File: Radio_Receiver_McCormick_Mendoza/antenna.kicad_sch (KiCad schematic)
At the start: 31 parts, among them J33 XFIL_IN, J34 XFIL_OUT, J45 CENTER_TAP, J5 Conn_Coaxial, J5 FIL_IN, J8 FIL_OUT, T1 Transformer_1P_SS, U13 SN74CBT3253CDBR

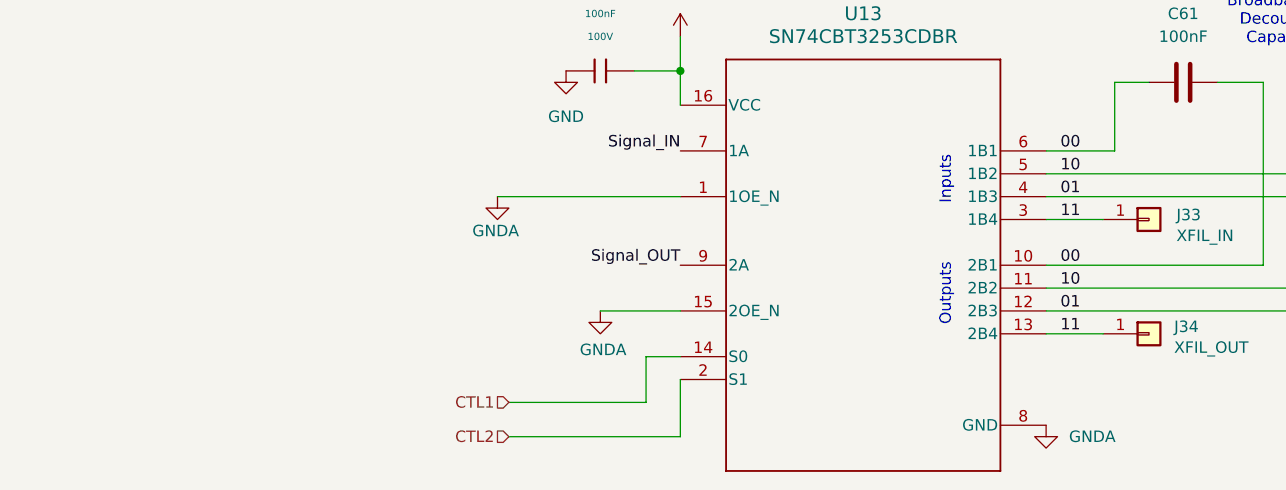
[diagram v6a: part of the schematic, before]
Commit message: Swapped voltage regulator to output 4.5V
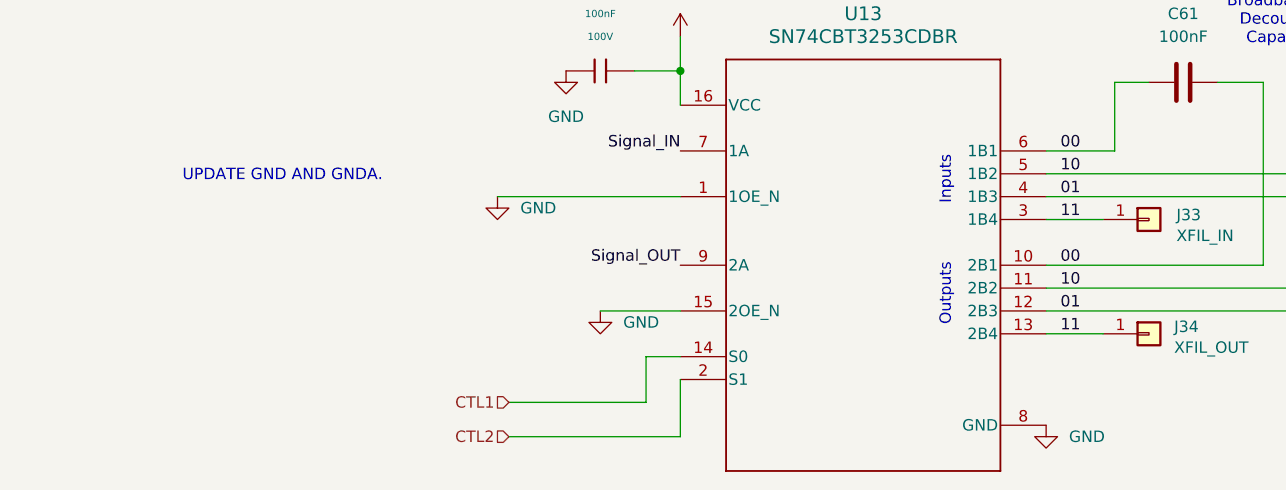
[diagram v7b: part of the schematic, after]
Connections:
- net GND: now also U13.1 (1OE_N), U13.15 (2OE_N), U13.8 (GND)
- net GNDA: no longer U13.1 (1OE_N), U13.15 (2OE_N), U13.8 (GND)
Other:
- note added: "UPDATE GND AND GNDA."
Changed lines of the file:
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@@
 		)
 	)
+	(text "UPDATE GND AND GNDA."
+		(exclude_from_sim no)
+		(at 62.484 118.364 0)
+		(effects
+			(font
+				(size 1.27 1.27)
+			)
+		)
+	)
 	(text "GNDA is the Antenna Ground\nIt must be separate from the\ndevice ground (GND) to prevent\nground loops."
 		(exclude_from_sim no)
@@
 	)
 	(symbol
-		(lib_id "power:GND")
-		(at 97.79 133.35 0)
-		(unit 1)
-		(body_style 1)
-		(exclude_from_sim no)
-		(in_bom yes)
-		(on_board yes)
-		(in_pos_files yes)
-		(dnp no)
-		(property "Reference" "#PWR012"
-			(at 97.79 139.7 0)
-			(hide yes)
-			(show_name no)
-			(do_not_autoplace no)
-			(effects
-				(font
-					(size 1.27 1.27)
-				)
-			)
-		)
-		(property "Value" "GNDA"
-			(at 95.504 137.668 0)
-			(show_name no)
-			(do_not_autoplace no)
-			(effects
-				(font
-					(size 1.27 1.27)
-				)
-				(justify left)
-			)
-		)
-		(property "Footprint" ""
-			(at 97.79 133.35 0)
-			(hide yes)
-			(show_name no)
-			(do_not_autoplace no)
-			(effects
-				(font
-					(size 1.27 1.27)
-				)
-			)
-		)
-		(property "Datasheet" ""
-			(at 97.79 133.35 0)
-			(hide yes)
-			(show_name no)
-			(do_not_autoplace no)
-			(effects
-				(font
-					(size 1.27 1.27)
-				)
-			)
-		)
-		(property "Description" "Power symbol creates a global label with name \"GND\" , ground"
-			(at 97.79 133.35 0)
-			(hide yes)
-			(show_name no)
-			(do_not_autoplace no)
-			(effects
-				(font
-					(size 1.27 1.27)
-				)
-			)
-		)
-		(pin "1"
-		)
-		(instances
-			(project "Radio_Receiver_McCormick_Mendoza"
-				(path "/f31d31ab-6846-4f3a-92b1-aa5a6a13373f/bb2f90fe-90d6-4041-8023-4e8a6153d0ef"
-					(reference "#PWR012")
-					(unit 1)
-				)
-			)
-		)
-	)
-	(symbol
 		(lib_id "SDRReciever-rescue:GND-power-SDRReciever-rescue")
 		(at 33.02 62.23 0)
@@
 	)
 	(symbol
+		(lib_id "power:GND")
+		(at 97.79 133.35 0)
+		(unit 1)
+		(body_style 1)
+		(exclude_from_sim no)
+		(in_bom yes)
+		(on_board yes)
+		(in_pos_files yes)
+		(dnp no)
+		(fields_autoplaced yes)
+		(property "Reference" "#PWR087"
+			(at 97.79 139.7 0)
+			(hide yes)
+			(show_name no)
+			(do_not_autoplace no)
+			(effects
+				(font
+					(size 1.27 1.27)
+				)
+			)
+		)
+		(property "Value" "GND"
+			(at 100.33 134.6199 0)
+			(show_name no)
+			(do_not_autoplace no)
+			(effects
+				(font
+					(size 1.27 1.27)
+				)
+				(justify left)
+			)
+		)
+		(property "Footprint" ""
+			(at 97.79 133.35 0)
+			(hide yes)
+			(show_name no)
+			(do_not_autoplace no)
+			(effects
+				(font
+					(size 1.27 1.27)
+				)
+			)
+		)
+		(property "Datasheet" ""
+			(at 97.79 133.35 0)
+			(hide yes)
+			(show_name no)
+			(do_not_autoplace no)
+			(effects
+				(font
+					(size 1.27 1.27)
+				)
+			)
+		)
+		(property "Description" "Power symbol creates a global label with name \"GND\" , ground"
+			(at 97.79 133.35 0)
+			(hide yes)
+			(show_name no)
+			(do_not_autoplace no)
+			(effects
+				(font
+					(size 1.27 1.27)
+				)
+			)
+		)
+		(pin "1"
+		)
+		(instances
+			(project "Radio_Receiver_McCormick_Mendoza"
+				(path "/f31d31ab-6846-4f3a-92b1-aa5a6a13373f/bb2f90fe-90d6-4041-8023-4e8a6153d0ef"
+					(reference "#PWR087")
+					(unit 1)
+				)
+			)
+		)
+	)
+	(symbol
+		(lib_id "power:GND")
+		(at 86.36 120.65 0)
+		(unit 1)
+		(body_style 1)
+		(exclude_from_sim no)
+		(in_bom yes)
+		(on_board yes)
+		(in_pos_files yes)
+		(dnp no)
+		(fields_autoplaced yes)
+		(property "Reference" "#PWR089"
+			(at 86.36 127 0)
+			(hide yes)
+			(show_name no)
+			(do_not_autoplace no)
+			(effects
+				(font
+					(size 1.27 1.27)
+				)
+			)
+		)
+		(property "Value" "GND"
+			(at 88.9 121.9199 0)
+			(show_name no)
+			(do_not_autoplace no)
+			(effects
+				(font
+					(size 1.27 1.27)
+				)
+				(justify left)
+			)
+		)
+		(property "Footprint" ""
+			(at 86.36 120.65 0)
+			(hide yes)
+			(show_name no)
+			(do_not_autoplace no)
+			(effects
+				(font
+					(size 1.27 1.27)
+				)
+			)
+		)
+		(property "Datasheet" ""
+			(at 86.36 120.65 0)
+			(hide yes)
+			(show_name no)
+			(do_not_autoplace no)
+			(effects
+				(font
+					(size 1.27 1.27)
+				)
+			)
+		)
+		(property "Description" "Power symbol creates a global label with name \"GND\" , ground"
+			(at 86.36 120.65 0)
+			(hide yes)
+			(show_name no)
+			(do_not_autoplace no)
+			(effects
+				(font
+					(size 1.27 1.27)
+				)
+			)
+		)
+		(pin "1"
+		)
+		(instances
+			(project "Radio_Receiver_McCormick_Mendoza"
+				(path "/f31d31ab-6846-4f3a-92b1-aa5a6a13373f/bb2f90fe-90d6-4041-8023-4e8a6153d0ef"
+					(reference "#PWR089")
+					(unit 1)
+				)
+			)
+		)
+	)
+	(symbol
 		(lib_id "SDRReciever-rescue:L-Device-SDRReciever-rescue")
 		(at 250.19 128.27 0)
@@
 			)
 		)
-		(property "Value" "GNDA"
+		(property "Value" "GND"
 			(at 149.86 147.3199 0)
 			(show_name no)
@@
 					(unit 1)
 				)
-			)
-		)
-	)
-	(symbol
-		(lib_id "power:GND")
-		(at 86.36 120.65 0)
-		(unit 1)
-		(body_style 1)
-		(exclude_from_sim no)
-		(in_bom yes)
-		(on_board yes)
-		(in_pos_files yes)
-		(dnp no)
-		(property "Reference" "#PWR09"
-			(at 86.36 127 0)
-			(hide yes)
-			(show_name no)
-			(do_not_autoplace no)
-			(effects
-				(font
-					(size 1.27 1.27)
-				)
-			)
-		)
-		(property "Value" "GNDA"
-			(at 83.566 124.46 0)
-			(show_name no)
-			(do_not_autoplace no)
-			(effects
-				(font
-					(size 1.27 1.27)
-				)
-				(justify left)
-			)
-		)
-		(property "Footprint" ""
-			(at 86.36 120.65 0)
-			(hide yes)
-			(show_name no)
-			(do_not_autoplace no)
-			(effects
-				(font
-					(size 1.27 1.27)
-				)
-			)
-		)
-		(property "Datasheet" ""
-			(at 86.36 120.65 0)
-			(hide yes)
-			(show_name no)
-			(do_not_autoplace no)
-			(effects
-				(font
-					(size 1.27 1.27)
-				)
-			)
-		)
-		(property "Description" "Power symbol creates a global label with name \"GND\" , ground"
-			(at 86.36 120.65 0)
-			(hide yes)
-			(show_name no)
-			(do_not_autoplace no)
-			(effects
-				(font
-					(size 1.27 1.27)
-				)
-			)
-		)
-		(pin "1"
-		)
-		(instances
-			(project "Radio_Receiver_McCormick_Mendoza"
-				(path "/f31d31ab-6846-4f3a-92b1-aa5a6a13373f/bb2f90fe-90d6-4041-8023-4e8a6153d0ef"
-					(reference "#PWR09")
-					(unit 1)
-				)

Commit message: Added the bnc connector footprint provided by dr Frohne
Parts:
- J5: footprint Connector_Coaxial:BNC_Amphenol_B6252HB-NPP3G-50_Horizontal -> Reciever_Parts:Conn_Coaxial_Frohne
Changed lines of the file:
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@@
 			)
 		)
-		(property "Footprint" "Connector_Coaxial:BNC_Amphenol_B6252HB-NPP3G-50_Horizontal"
+		(property "Footprint" "Reciever_Parts:Conn_Coaxial_Frohne"
 			(at 33.02 40.64 0)
 			(hide yes)
